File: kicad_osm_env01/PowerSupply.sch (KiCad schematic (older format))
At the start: 59 parts

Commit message: kicad review sch initial
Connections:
- net 5V_IN renamed 5Vin
- net BAT_MON renamed BatMon
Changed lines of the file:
@@
 $Descr A4 11693 8268
 encoding utf-8
-Sheet 3 9
+Sheet 2 9
 Title ""
 Date ""
@@
 	3575 1225 5075 1225
 Wire Wire Line
-	1175 1625 1575 1625
+	1175 1625 1300 1625
 Wire Wire Line
 	3575 2825 3575 3525
@@
 	0    1    -1   0
 $EndComp
-Text Label 1175 1625 0    50   ~ 0
-5V_IN
 Wire Wire Line
 	1575 1625 1575 2325
@@
 	9300 5100 9650 5100
 Connection ~ 9300 5100
-Text Label 9650 5100 2    50   ~ 0
-BAT_MON
 $Comp
 L OSM_env01-rescue:GND-ESP32-EVB_Rev_D #PWR?
@@
 Wire Notes Line
 	6650 4525 6675 550
+Text HLabel 1225 1725 0    50   Input ~ 0
+5Vin
+Wire Wire Line
+	1225 1725 1300 1725
+Wire Wire Line
+	1300 1725 1300 1625
+Connection ~ 1300 1625
+Wire Wire Line
+	1300 1625 1575 1625
+Text HLabel 4100 5500 2    50   Input ~ 0
+5Vout
+Text HLabel 6500 5825 2    50   Input ~ 0
+3.3Vout
+Wire Wire Line
+	4100 5500 4050 5500
+Wire Wire Line
+	4050 5500 4050 5825
+Text HLabel 9475 4975 2    50   Input ~ 0
+BatMon
+Wire Wire Line
+	9475 4975 9300 4975
+Wire Wire Line
+	9300 4975 9300 5100
 $EndSCHEMATC

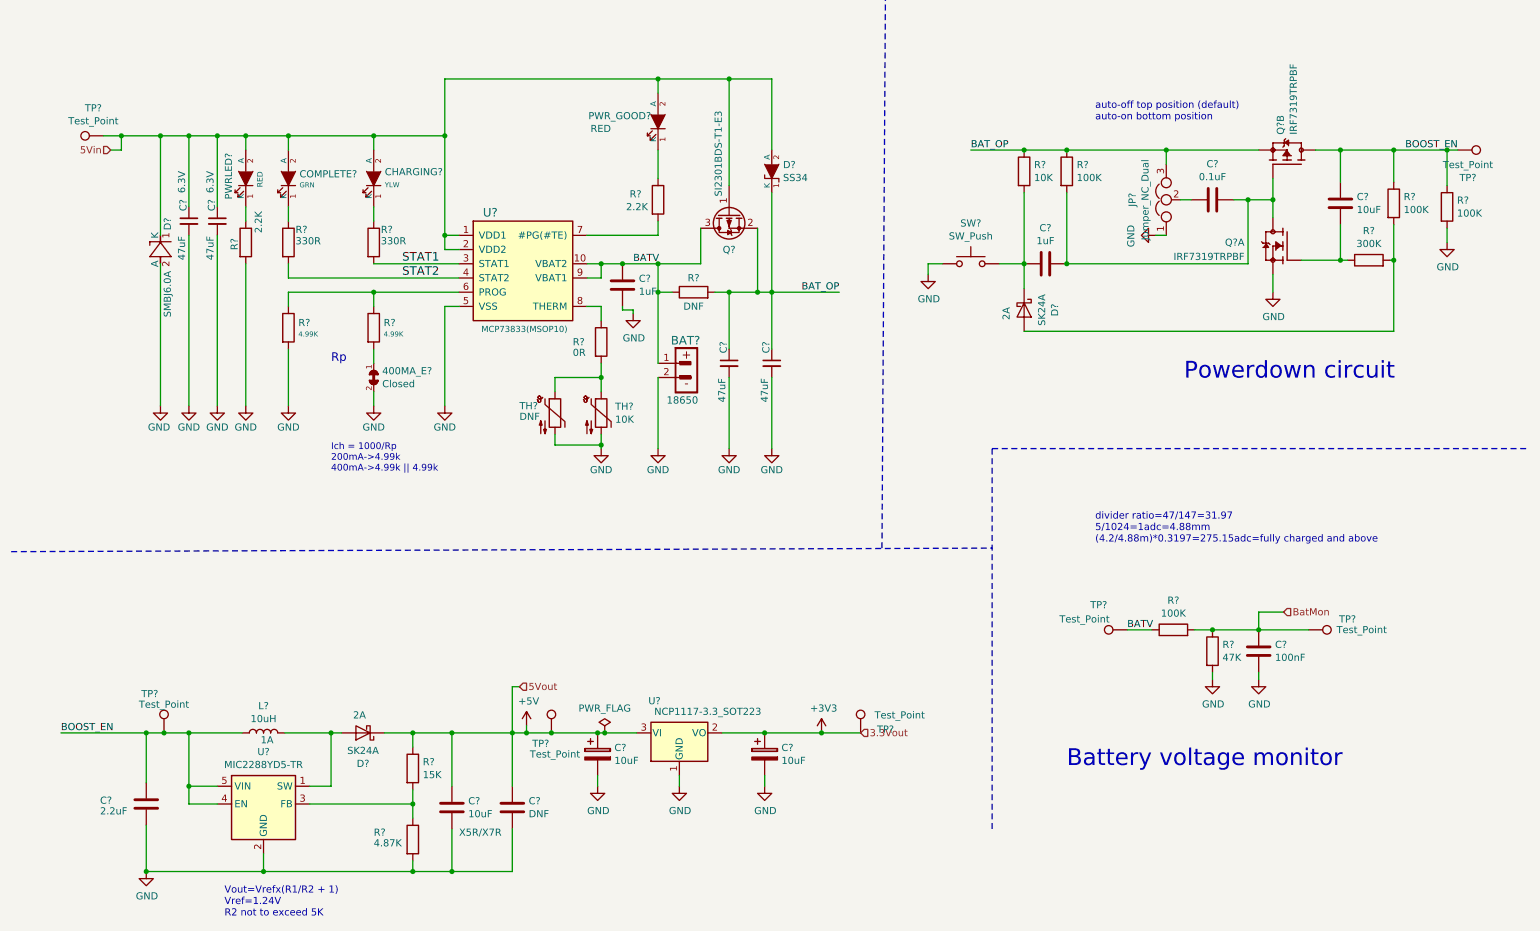
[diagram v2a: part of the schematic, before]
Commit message: updated schematics
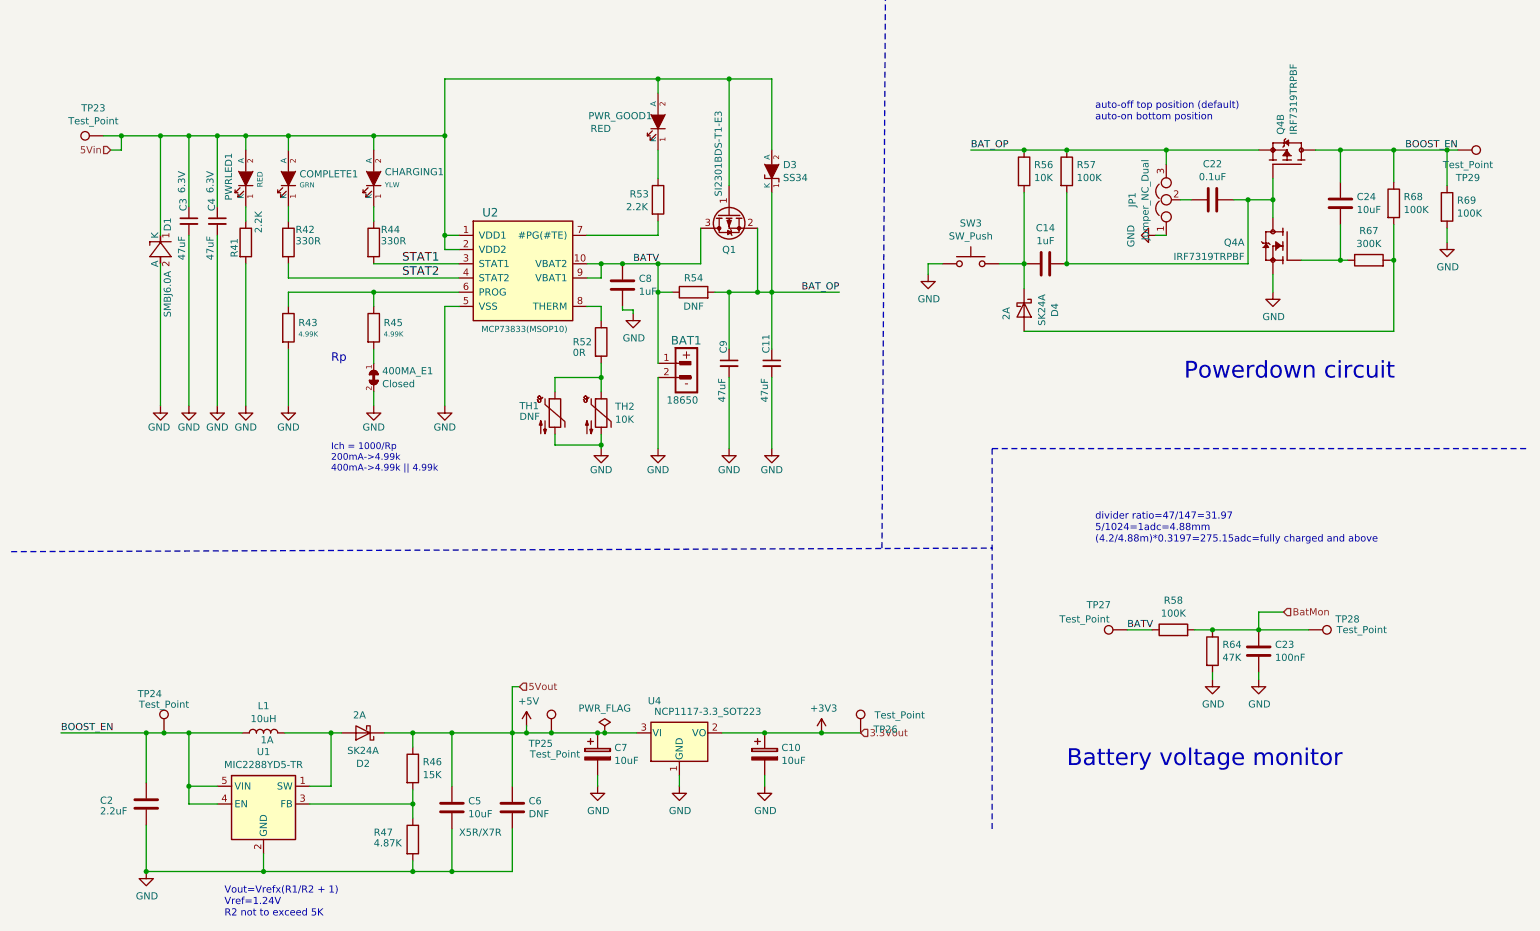
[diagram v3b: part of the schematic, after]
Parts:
- gave numbers to parts that had none: 58

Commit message: schematics awaiting review
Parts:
- removed TP24: Test_Point, TestPoint:TestPoint_THTPad_D1.0mm_Drill0.5mm, symbol OSM_env01-rescue:Test_Point-Connector-ESP32-EVB_Rev_D-rescue
- added TP79: Test_Point, TestPoint:TestPoint_THTPad_D1.0mm_Drill0.5mm, symbol OSM_env01-rescue:Test_Point-Connector-ESP32-EVB_Rev_D-rescue
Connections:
- net BAT_OP: now also TP79.1
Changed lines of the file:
@@
 	1475 6175 1475 5825
-Wire Wire Line
-	1475 5825 1600 5825
 Wire Wire Line
 	3625 6200 3625 5825
@@
 $EndComp
 $Comp
-L OSM_env01-rescue:Test_Point-Connector-ESP32-EVB_Rev_D-rescue TP24
-U 1 1 607F8D01
-P 1600 5825
-F 0 "TP24" H 1500 6100 50  0000 C CNN
-F 1 "Test_Point" H 1600 6025 50  0000 C CNN
-F 2 "TestPoint:TestPoint_THTPad_D1.0mm_Drill0.5mm" H 1800 5825 50  0001 C CNN
-F 3 "~" H 1800 5825 50  0001 C CNN
-	1    1600 5825
-	1    0    0    -1
-$EndComp
-Connection ~ 1600 5825
-Wire Wire Line
-	1600 5825 1775 5825
-$Comp
 L OSM_env01-rescue:Test_Point-Connector-ESP32-EVB_Rev_D-rescue TP25
 U 1 1 607F8D09
@@
 Wire Wire Line
 	4325 5825 4650 5825
-$Comp
-L OSM_env01-rescue:Test_Point-Connector-ESP32-EVB_Rev_D-rescue TP26
-U 1 1 607F8D11
-P 6500 5825
-F 0 "TP26" H 6675 5850 50  0000 C CNN
-F 1 "Test_Point" H 6775 5950 50  0000 C CNN
-F 2 "TestPoint:TestPoint_THTPad_D1.0mm_Drill0.5mm" H 6700 5825 50  0001 C CNN
-F 3 "~" H 6700 5825 50  0001 C CNN
-	1    6500 5825
-	1    0    0    -1
-$EndComp
 Connection ~ 5825 5825
 Wire Wire Line
@@
 Connection ~ 6225 5825
 Wire Wire Line
-	6225 5825 6500 5825
+	6225 5825 6450 5825
 $Comp
 L power:PWR_FLAG #FLG01
@@
 	0    -1   -1   0
 $EndComp
-$Comp
-L OSM_env01-rescue:Test_Point-Connector-ESP32-EVB_Rev_D-rescue TP28
-U 1 1 607F8DF8
-P 9650 5100
-F 0 "TP28" V 9575 5375 50  0000 C CNN
-F 1 "Test_Point" V 9650 5475 50  0000 C CNN
-F 2 "TestPoint:TestPoint_THTPad_D1.0mm_Drill0.5mm" H 9850 5100 50  0001 C CNN
-F 3 "~" H 9850 5100 50  0001 C CNN
-	1    9650 5100
-	0    1    1    0
-$EndComp
 Wire Wire Line
 	9225 2075 9225 2525
@@
 U 1 1 607F8E24
 P 10700 1725
-F 0 "TP29" V 10895 1797 50  0000 C CNN
-F 1 "Test_Point" V 10804 1797 50  0000 C CNN
+F 0 "TP29" V 10700 2000 50  0000 C CNN
+F 1 "Test_Point" V 10804 1797 50  0001 C CNN
 F 2 "TestPoint:TestPoint_THTPad_D1.0mm_Drill0.5mm" H 10900 1725 50  0001 C CNN
 F 3 "~" H 10900 1725 50  0001 C CNN
@@
 Wire Wire Line
 	9300 4975 9300 5100
+$Comp
+L OSM_env01-rescue:Test_Point-Connector-ESP32-EVB_Rev_D-rescue TP79
+U 1 1 608245C5
+P 6350 2725
+F 0 "TP79" V 6350 3000 50  0000 C CNN
+F 1 "Test_Point" V 6454 2797 50  0001 C CNN
+F 2 "TestPoint:TestPoint_THTPad_D1.0mm_Drill0.5mm" H 6550 2725 50  0001 C CNN
+F 3 "~" H 6550 2725 50  0001 C CNN
+	1    6350 2725
+	0    1    1    0
+$EndComp
+Wire Wire Line
+	1475 5825 1775 5825
+$Comp
+L OSM_env01:PWR_FLAG #FLG0104
+U 1 1 606ED67C
+P 3575 1075
+F 0 "#FLG0104" H 3575 1170 50  0001 C CNN
+F 1 "PWR_FLAG" H 3575 1298 50  0000 C CNN
+F 2 "" H 3575 1075 60  0000 C CNN
+F 3 "" H 3575 1075 60  0000 C CNN
+	1    3575 1075
+	1    0    0    -1
+$EndComp
+Wire Wire Line
+	3575 1225 3575 1075
+Connection ~ 3575 1225
+$Comp
+L OSM_env01-rescue:Test_Point-Connector-ESP32-EVB_Rev_D-rescue TP?
+U 1 1 60A59EE0
+P 6450 5825
+AR Path="/5F6F7717/60A59EE0" Ref="TP?"  Part="1"
+AR Path="/60A59EE0" Ref="TP?"  Part="1"
+AR Path="/608F4675/60A59EE0" Ref="TP?"  Part="1"
+AR Path="/60688D25/60A59EE0" Ref="TP26"  Part="1"
+F 0 "TP26" V 6450 6100 50  0000 C CNN
+F 1 "Test_Point" V 6525 6050 50  0001 C CNN
+F 2 "TestPoint:TestPoint_THTPad_D1.0mm_Drill0.5mm" H 6650 5825 50  0001 C CNN
+F 3 "~" H 6650 5825 50  0001 C CNN
+	1    6450 5825
+	1    0    0    -1
+$EndComp
+Connection ~ 6450 5825
+Wire Wire Line
+	6450 5825 6500 5825
+$Comp
+L OSM_env01-rescue:Test_Point-Connector-ESP32-EVB_Rev_D-rescue TP?
+U 1 1 60A6B22E
+P 9650 5100
+AR Path="/5F6F7717/60A6B22E" Ref="TP?"  Part="1"
+AR Path="/60A6B22E" Ref="TP?"  Part="1"
+AR Path="/608F4675/60A6B22E" Ref="TP?"  Part="1"
+AR Path="/60688D25/60A6B22E" Ref="TP28"  Part="1"
+F 0 "TP28" V 9650 5375 50  0000 C CNN
+F 1 "Test_Point" V 9725 5325 50  0001 C CNN
+F 2 "TestPoint:TestPoint_THTPad_D1.0mm_Drill0.5mm" H 9850 5100 50  0001 C CNN
+F 3 "~" H 9850 5100 50  0001 C CNN
+	1    9650 5100
+	0    1    1    0
+$EndComp
 $EndSCHEMATC

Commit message: updated schematics
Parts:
- added C72: DNF, symbol device:C
- added D10: D, symbol device:D
- added R127: DNF, symbol device:R
- added R128: 0R, symbol device:R
- R69: footprint (none) -> Resistor_SMD:R_0603_1608Metric
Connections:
- net BAT_OP: now also R127.1
- net BOOST_EN: now also C72.1
- net at C14.2, C22.2, Q4.7 (D)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: now also D10.2 (A), R128.2; no longer Q4.4 (G)
- new net: C72.2, D10.1 (K), Q4.4 (G), R127.2, R128.1
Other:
- moved on the sheet: 400MA_E1, BAT1, C11, C14, C22, C24, C3, C4, C8, C9, CHARGING1, COMPLETE1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

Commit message: started layout
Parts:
- C72: footprint (none) -> Capacitor_SMD:C_0603_1608Metric
- D10: footprint (none) -> Diode_SMD:D_SOD-123
- R127, R128: footprint (none) -> Resistor_SMD:R_0603_1608Metric
- U2: footprint Devtank_PCB_lib:MCP8833-AMI_UN -> Devtank_PCB_lib:MCP73833-AMI_UN_buck_converter
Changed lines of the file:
@@
 $Descr A3 16535 11693
 encoding utf-8
-Sheet 2 12
+Sheet 2 11
 Title ""
 Date ""
@@
 F 0 "U2" H 3445 3060 60  0000 C CNN
 F 1 "MCP73833(MSOP10)" H 3685 2240 43  0000 C CNN
-F 2 "Devtank_PCB_lib:MCP8833-AMI_UN" H 3725 2600 60  0001 C CNN
+F 2 "Devtank_PCB_lib:MCP73833-AMI_UN_buck_converter" H 3725 2600 60  0001 C CNN
 F 3 "" H 3725 2600 60  0001 C CNN
 F 4 "Value 1" H 3625 2600 60  0001 C CNN "Fieldname 1"
@@
 F 0 "R128" H 11645 1996 50  0000 L CNN
 F 1 "0R" H 11645 1905 50  0000 L CNN
-F 2 "" V 11505 1950 50  0001 C CNN
+F 2 "Resistor_SMD:R_0603_1608Metric" V 11505 1950 50  0001 C CNN
 F 3 "" H 11575 1950 50  0001 C CNN
 	1    11575 1950
@@
 F 0 "C72" V 11823 1725 50  0000 C CNN
 F 1 "DNF" V 11914 1725 50  0000 C CNN
-F 2 "" H 12113 1575 50  0001 C CNN
+F 2 "Capacitor_SMD:C_0603_1608Metric" H 12113 1575 50  0001 C CNN
 F 3 "" H 12075 1725 50  0001 C CNN
 	1    12075 1725
@@
 F 0 "R127" H 10945 1621 50  0000 L CNN
 F 1 "DNF" H 10945 1530 50  0000 L CNN
-F 2 "" V 10805 1575 50  0001 C CNN
+F 2 "Resistor_SMD:R_0603_1608Metric" V 10805 1575 50  0001 C CNN
 F 3 "" H 10875 1575 50  0001 C CNN
 	1    10875 1575
@@
 F 0 "D10" V 11129 2004 50  0000 L CNN
 F 1 "D" V 11220 2004 50  0000 L CNN
-F 2 "" H 11175 1925 50  0001 C CNN
+F 2 "Diode_SMD:D_SOD-123" H 11175 1925 50  0001 C CNN
 F 3 "" H 11175 1925 50  0001 C CNN
 	1    11175 1925

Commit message: Throwdown of parts
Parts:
- 400MA_E1: symbol OSM_env01-rescue:SJ_Closed-ESP32-EVB_Rev_D -> device:Jumper_NC_Small
- BAT1: symbol OSM_env01-rescue:BAT_CON-ESP32-EVB_Rev_D -> device:Battery
- C11, C3, C4, C9: symbol OSM_env01-rescue:C-ESP32-EVB_Rev_D -> device:C
- C24: footprint Capacitor_SMD:C_0603_1608Metric -> Capacitor_SMD:C_0805_2012Metric
- C8: symbol OSM_env01-rescue:C-device-ESP32-EVB_Rev_D-rescue -> device:C
- CHARGING1, COMPLETE1, PWRLED1, PWR_GOOD1: symbol OSM_env01-rescue:LED-ESP32-EVB_Rev_D -> device:LED
- D1: symbol OSM_env01-rescue:SMBJ6.0A-ESP32-EVB_Rev_D -> device:D_Zener
- D3: symbol OSM_env01-rescue:D_Schottky-ESP32-EVB_Rev_D -> device:D_Schottky
- D4: footprint Diode_SMD:D_SMA -> Diode_SMD:D_SOD-123
- U4: value NCP1117-3.3_SOT223 -> NCP1117ST33T3G
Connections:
- net GND: now also 400MA_E1.1; no longer 400MA_E1.2
- net at R45.2: now also 400MA_E1.2; no longer 400MA_E1.1
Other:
- moved on the sheet: BAT1, C11, C3, C4, C8, C9, Q1, R41, R42, R43, R44, R45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

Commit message: schematics awaiting review
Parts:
- removed 400MA_E1: Closed, Connector_PinHeader_1.27mm:PinHeader_1x02_P1.27mm_Vertical, symbol device:Jumper_NC_Small
- removed JP1: Jumper_NC_Dual, Connector_PinHeader_1.27mm:PinHeader_1x03_P1.27mm_Vertical, symbol OSM_env01-rescue:Jumper_NC_Dual-device-ESP32-EVB_Rev_D-rescue
- removed TP23: Test_Point, TestPoint:TestPoint_THTPad_D1.0mm_Drill0.5mm, symbol OSM_env01-rescue:Test_Point-Connector-ESP32-EVB_Rev_D-rescue
- added R18, R21: 100K, symbol device:R
- added R19, R22: 47K, symbol device:R
- added R27: 0R, symbol device:R
- added R28: DNF, symbol device:R
- added TP18: Test_Point, TestPoint:TestPoint_THTPad_D1.0mm_Drill0.5mm, symbol OSM_env01-rescue:Test_Point-Connector-ESP32-EVB_Rev_D-rescue
- C2: value 2.2uF -> 4.7uF
- C5: value 10uF -> 22uF
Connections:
- net +3V3: now also R18.1
- net +5V: now also R21.1
- net BATV: now also TP18.1
- net BAT_OP: now also R27.1
- net GND: now also R45.2, R19.2, R22.2, R28.2
- net at C22.1: now also R27.2, R28.1
- new net 3V3_RAIL_MON: R18.2, R19.1
- new net 5V_RAIL_MON: R21.2, R22.1
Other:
- note added: "5V and 3V3 Power Supplies\n\n\n"
- note added: "Battery Voltage Monitor\n\n\n"
- note added: "Latched powerbutton Circuit\n\n"
- note added: "Li_Ion Battery Charge Controller\n\n"
- note added: "Note: If MIC2250 used R1 should be as large as poosible ideally around 100k\n"
- note added: "Voltage Rail Monitor\n\n\n"
- note removed: "Battery voltage monitor"
- note removed: "Powerdown circuit\n"
- moved on the sheet: C10, C14, C2, C22, C23, C24, C5, C6, C7, C72, D10, D2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
